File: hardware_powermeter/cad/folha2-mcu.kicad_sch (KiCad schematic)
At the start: 14 parts, among them J201 Tag-Connect TC2030-NL, U201 MinewSemi ME54BS13

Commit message: feat(hardware): 48 x 16 mm board and a 53,4 x 19,4 x 8,5 mm pod
The board came down from 60 to 48 mm and the pod from 65,4 x 19,4 x 10,5
to 53,4 x 19,4 x 8,5, with the mass estimate at 11,4 g against the 20 g
of the class. The height now meets the target exactly, because the cell
shrank from 4,0 to 2,5 mm: the owner's 5 kOhm decision takes the meter
from 3,9 to 1,5 mA while pedalling, so 50 hours ask for about 75 mAh and
a 100 mAh pouch is enough. The six-way connector stays, in two rows of
three instead of a single row, which gave back about 7 mm of length
without losing a way, and the Tag-Connect went: with SWD on the cable it
was duplicated copper.

It is NOT manufacturable yet, and the numbers say why rather than a
hopeful adjective: the design rule check finds 0 errors but 16
connections still open. One of them, ERR_N, has no copper at all while
the router reported "98 routed, 0 nets left out", so the router's own
accounting is wrong, not just its routing. Disabling the pruning of
dangling tracks was tried first and changed nothing, which clears the
pruning. A second routing pass made it worse, 21 open and three pairs of
vias too close: the pass is not incremental, it re-routes from scratch
into a different result.

Two more real defects are recorded: the placer cannot seat C403 and
C308, carrying them 11 to 13 mm from the part they decouple, and three
pod rules fail, the back-face bodies against the cell, the rib at zero
and a back pad under a pillar.

The layer drawings print properly for the first time. kicad-cli 8.0.6
does not have --page-size-mode or --exclude-drawing-sheet, which are
KiCad 9 options, so the export was failing outright and, before that,
putting a 1:1 board in the corner of an empty sheet. The flags are now
tried and dropped if unknown, and the board is cropped with fitz
instead: 5:1, centred, scale bar and title block.
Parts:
- removed J201: Tag-Connect TC2030-NL, Connector:Tag-Connect_TC2030-IDC-NL_2x03_P1.27mm_Vertical, symbol pmeter:J201
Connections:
- net RESET: no longer names the net of U201.4 (RESET)
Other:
- note added: "2 MCU e depuracao - 13 posicoes. NADA MONTADO NEM MEDIDO."
- note removed: "2 MCU e depuracao - 14 posicoes. NADA MONTADO NEM MEDIDO."
- moved on the sheet: D201, R201, R202, R203

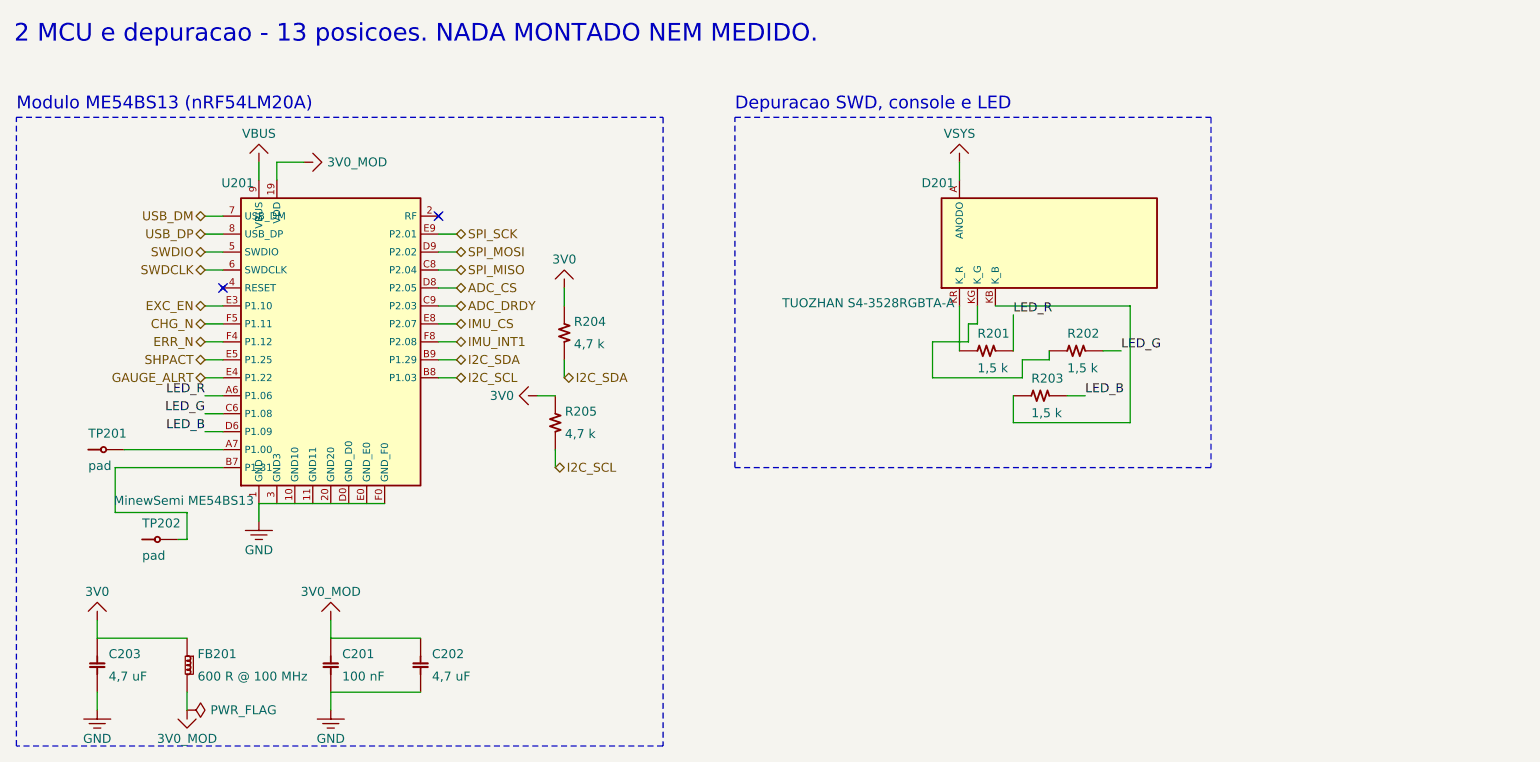
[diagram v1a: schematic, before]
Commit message: feat(hardware): draw the module for real, and bond the pod to flat metal
Two things the owner asked for, and one the second of them found.

The module gets a body instead of a box. Every DIMENSION is off the maker's
mechanical drawing - the one the footprint is generated from, which closes on
itself three independent ways - and every COLOUR is read off the product
photo, and that difference is recorded rather than smoothed over: a dimension
that closes three ways is evidence, a colour from a photograph is a reading.
It is not one box, because the part is not one box and drawing it as one
hides what decides the layout: a BLACK printed circuit (Holyiot's photo, not
the green of the ME54BS13), a shield can that reads dark rather than as
bright tin, the CERAMIC ANTENNA as an ivory block with metallised ends
sitting outside the can in the 3,80 mm band the drawing keeps clear of pads,
and the gold pads on the underside. Forty-one solids.

It is drawn 2,40 mm tall, and that is a RESERVATION, not a measurement: the
advert gives no height at all. A can over a 0,80 mm board runs 1,8 to 2,2 in
this class, so 2,40 has margin, and drawing it at the reservation makes the
body, the lid's ceiling and the new rule PD18 carry the same number - a part
that arrives taller is then caught by a rule instead of by a lid that will
not close.

The owner asked for the open questions to be measured rather than waited for,
so each one became a requirement with a rule that checks it. The crank's
numbers are the CLASS's - Shimano 105 and Ultegra, the narrow end of the
arm's taper, the tight end of road frame clearance - and PD17 measures the
pod against them. It failed on the first run, and the finding is real: the
arm's inner face is not flat across. A fillet of about 2,5 mm on each side
leaves only 15 of the class's 20 mm flat, and a 19,0 mm pod bonded across its
whole underside would sit on those radii on both sides - adhesive thick at
the edges, thin in the middle, and a joint that peels from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
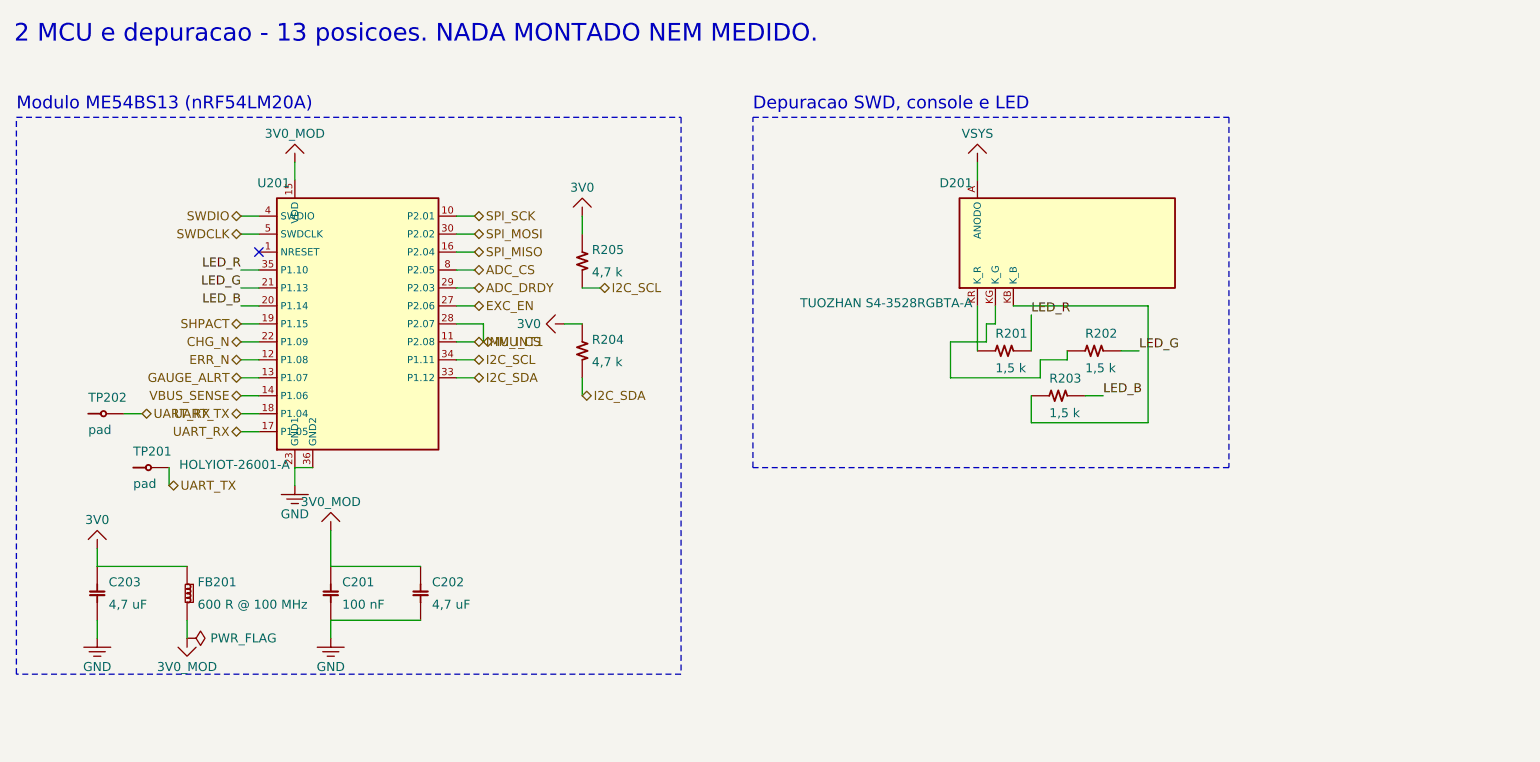
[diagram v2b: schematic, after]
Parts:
- U201: value MinewSemi ME54BS13 -> HOLYIOT-26001-A; footprint pmeter:MinewSemi_ME54BS13_16.5x12mm -> pmeter:HOLYIOT_26001A_10x12.5mm
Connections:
- net USB_DP is gone; now on net ADC_CS: U201.8 (P2.05)
- net 3V0_MOD: now also U201.15 (VDD); no longer U201.19 (VDD)
- net ADC_CS: no longer U201.D8 (P2.05)
- net ADC_DRDY: now also U201.29 (P2.03); no longer U201.C9 (P2.03)
- net CHG_N: now also U201.22 (P1.09); no longer U201.F5 (P1.11)
- net ERR_N: now also U201.12 (P1.08); no longer U201.F4 (P1.12)
- net EXC_EN: now also U201.27 (P2.06); no longer U201.E3 (P1.10)
- net GAUGE_ALRT: now also U201.13 (P1.07); no longer U201.E4 (P1.22)
- net GND: now also U201.23 (GND1), U201.36 (GND2); no longer U201.1 (GND), U201.10 (GND10), U201.11 (GND11), U201.20 (GND20), U201.3 (GND3), U201.D0 (GND_D0), U201.E0 (GND_E0), U201.F0 (GND_F0)
- net I2C_SCL: now also U201.34 (P1.11); no longer U201.B8 (P1.03)
- net I2C_SDA: now also U201.33 (P1.12); no longer U201.B9 (P1.29)
- net IMU_CS: now also U201.28 (P2.07); no longer U201.E8 (P2.07)
- net IMU_INT1: now also U201.11 (P2.08); no longer U201.F8 (P2.08)
- net LED_B: now also U201.20 (P1.14); no longer U201.D6 (P1.09)
- net LED_G: now also U201.21 (P1.13); no longer U201.C6 (P1.08)
- net LED_R: now also U201.35 (P1.10); no longer U201.A6 (P1.06)
- net SHPACT: now also U201.19 (P1.15); no longer U201.E5 (P1.25)
- net SPI_MISO: now also U201.16 (P2.04); no longer U201.C8 (P2.04)
- net SPI_MOSI: now also U201.30 (P2.02); no longer U201.D9 (P2.02)
- net SPI_SCK: now also U201.10 (P2.01); no longer U201.E9 (P2.01)
- net SWDCLK: now also U201.5 (SWDCLK); no longer U201.6 (SWDCLK)
- net SWDIO: now also U201.4 (SWDIO); no longer U201.5 (SWDIO)
- net UART_TX: now reaches TP201.1
- net UART_TX: now also U201.18 (P1.04); no longer U201.A7 (P1.00)
- net UART_RX: now reaches TP202.1
- net UART_RX: now also U201.17 (P1.05); no longer U201.B7 (P1.31)
- removed net USB_DM: U201.7 (USB_DM)
- removed net VBUS: U201.9 (VBUS)
- new net VBUS_SENSE: U201.14 (P1.06)
- no-connect marks 2 -> 1
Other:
- moved on the sheet: C201, C202, C203, D201, FB201, R201, R202, R203, R204, R205, TP201, TP202
